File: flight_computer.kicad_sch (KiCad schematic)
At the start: 2 parts

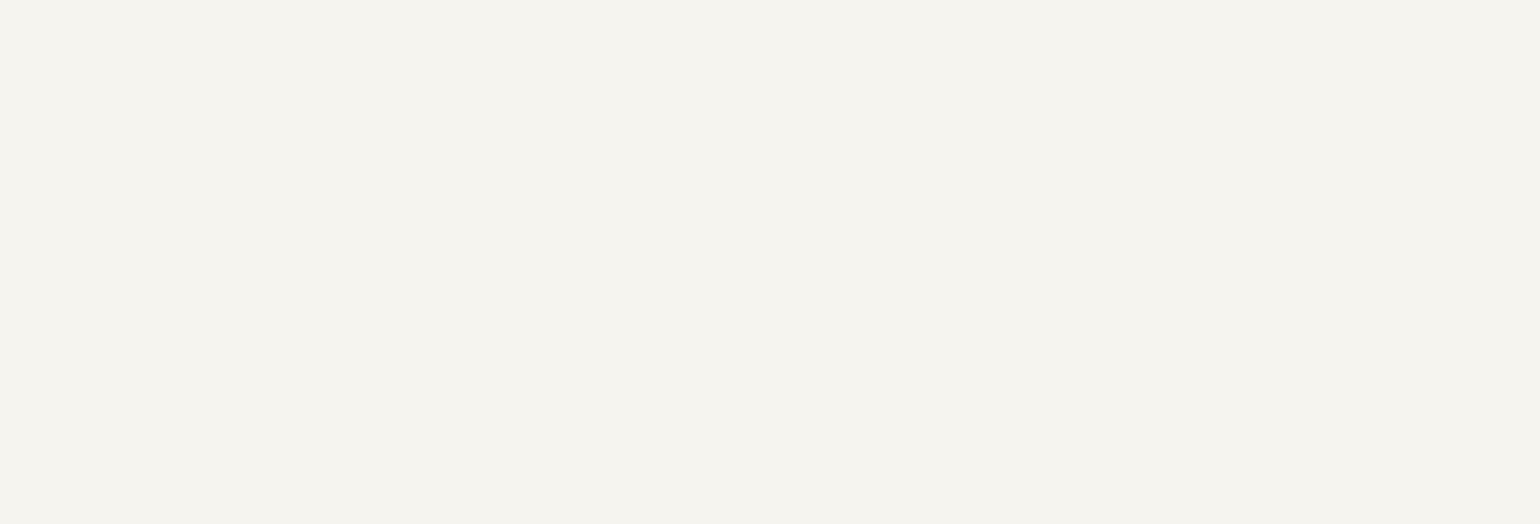
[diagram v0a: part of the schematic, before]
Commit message: Major fix: move from a flat to a hierarchical architecture for schematic.
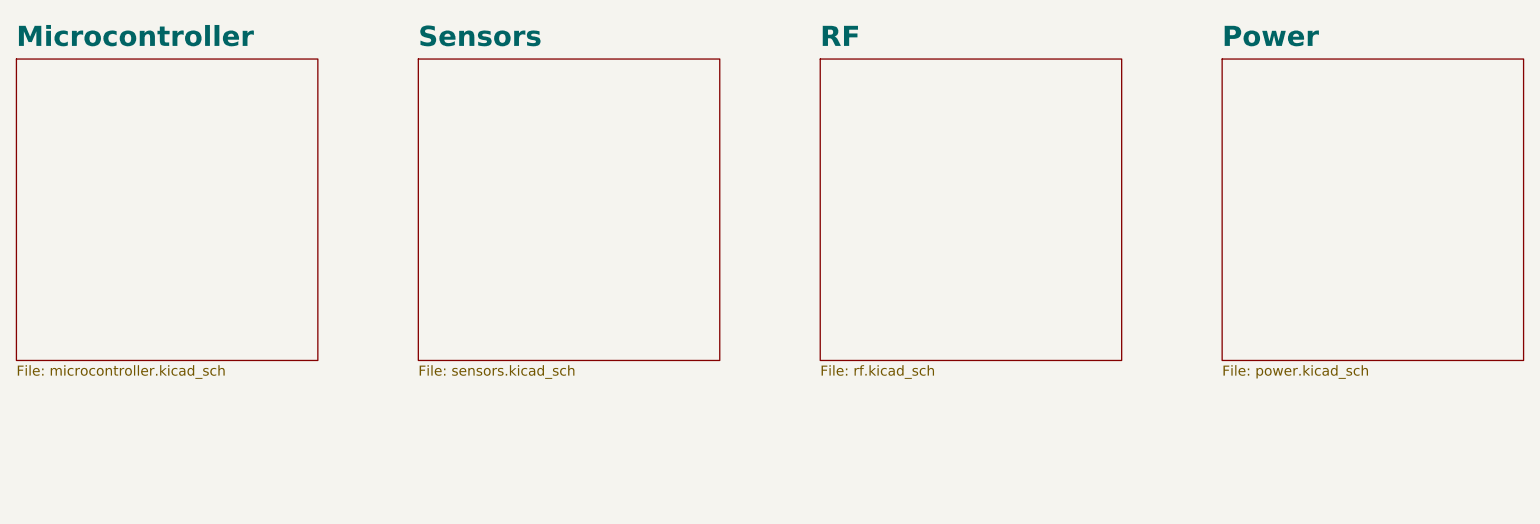
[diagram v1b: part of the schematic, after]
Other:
- added sheet Microcontroller (microcontroller.kicad_sch)
- added sheet Power (power.kicad_sch)
- added sheet RF (rf.kicad_sch)
- added sheet Sensors (sensors.kicad_sch)
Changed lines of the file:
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@@
+		)
+	)
+	(sheet
+		(at 177.8 25.4)
+		(size 38.1 38.1)
+		(exclude_from_sim no)
+		(in_bom yes)
+		(on_board yes)
+		(dnp no)
+		(fields_autoplaced yes)
+		(stroke
+			(width 0.1524)
+			(type solid)
+		)
+		(fill
+			(color 0 0 0 0)
+		)
+		(property "Sheetname" "Power"
+			(at 177.8 24.0534 0)
+			(show_name no)
+			(do_not_autoplace no)
+			(effects
+				(font
+					(size 2.54 2.54)
+					(thickness 0.508)
+					(bold yes)
+				)
+				(justify left bottom)
+			)
+		)
+		(property "Sheetfile" "power.kicad_sch"
+			(at 177.8 64.0846 0)
+			(show_name no)
+			(do_not_autoplace no)
+			(effects
+				(font
+					(size 1.27 1.27)
+				)
+				(justify left top)
+			)
+		)
+		(instances
+			(project "flight_computer"
+				(path "/aee43b18-7cf7-43bb-b265-763f492d287e"
+					(page "2")
+				)
+			)
+		)
+	)
+	(sheet
+		(at 25.4 25.4)
+		(size 38.1 38.1)
+		(exclude_from_sim no)
+		(in_bom yes)
+		(on_board yes)
+		(dnp no)
+		(fields_autoplaced yes)
+		(stroke
+			(width 0.1524)
+			(type solid)
+		)
+		(fill
+			(color 0 0 0 0)
+		)
+		(property "Sheetname" "Microcontroller"
+			(at 25.4 24.0534 0)
+			(show_name no)
+			(do_not_autoplace no)
+			(effects
+				(font
+					(size 2.54 2.54)
+					(thickness 0.508)
+					(bold yes)
+				)
+				(justify left bottom)
+			)
+		)
+		(property "Sheetfile" "microcontroller.kicad_sch"
+			(at 25.4 64.0846 0)
+			(show_name no)
+			(do_not_autoplace no)
+			(effects
+				(font
+					(size 1.27 1.27)
+				)
+				(justify left top)
+			)
+		)
+		(instances
+			(project "flight_computer"
+				(path "/aee43b18-7cf7-43bb-b265-763f492d287e"
+					(page "3")
+				)
+			)
+		)
+	)
+	(sheet
+		(at 76.2 25.4)
+		(size 38.1 38.1)
+		(exclude_from_sim no)
+		(in_bom yes)
+		(on_board yes)
+		(dnp no)
+		(fields_autoplaced yes)
+		(stroke
+			(width 0.1524)
+			(type solid)
+		)
+		(fill
+			(color 0 0 0 0)
+		)
+		(property "Sheetname" "Sensors"
+			(at 76.2 24.0534 0)
+			(show_name no)
+			(do_not_autoplace no)
+			(effects
+				(font
+					(size 2.54 2.54)
+					(thickness 0.508)
+					(bold yes)
+				)
+				(justify left bottom)
+			)
+		)
+		(property "Sheetfile" "sensors.kicad_sch"
+			(at 76.2 64.0846 0)
+			(show_name no)
+			(do_not_autoplace no)
+			(effects
+				(font
+					(size 1.27 1.27)
+				)
+				(justify left top)
+			)
+		)
+		(instances
+			(project "flight_computer"
+				(path "/aee43b18-7cf7-43bb-b265-763f492d287e"
+					(page "4")
+				)
+			)
+		)
+	)
+	(sheet
+		(at 127 25.4)
+		(size 38.1 38.1)
+		(exclude_from_sim no)
+		(in_bom yes)
+		(on_board yes)
+		(dnp no)
+		(fields_autoplaced yes)
+		(stroke
+			(width 0.1524)
+			(type solid)
+		)
+		(fill
+			(color 0 0 0 0)
+		)
+		(property "Sheetname" "RF"
+			(at 127 24.0534 0)
+			(show_name no)
+			(do_not_autoplace no)
+			(effects
+				(font
+					(size 2.54 2.54)
+					(thickness 0.508)
+					(bold yes)
+				)
+				(justify left bottom)
+			)
+		)
+		(property "Sheetfile" "rf.kicad_sch"
+			(at 127 64.0846 0)
+			(show_name no)
+			(do_not_autoplace no)
+			(effects
+				(font
+					(size 1.27 1.27)
+				)
+				(justify left top)
+			)
+		)
+		(instances
+			(project "flight_computer"
+				(path "/aee43b18-7cf7-43bb-b265-763f492d287e"
+					(page "5")
+				)
+			)
 		)
 	)

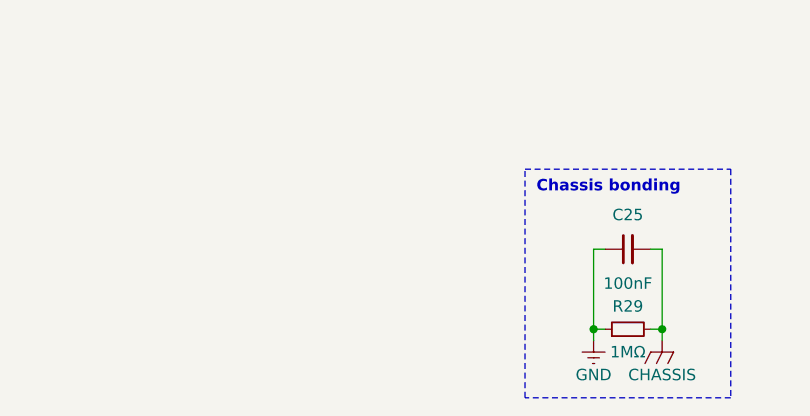
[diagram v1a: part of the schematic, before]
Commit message: Added M3 mounting holes to schematic, replaced them in PCB layout so they appear in the output documents
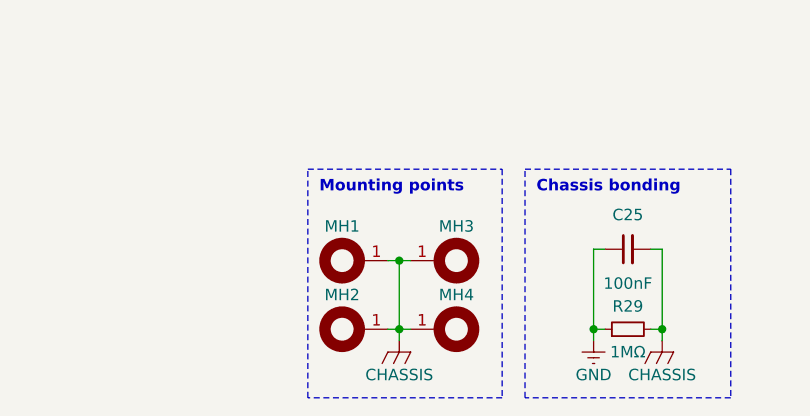
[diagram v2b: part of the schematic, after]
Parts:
- added MH1, MH2, MH3, MH4: (no value), miscellaneous:M3, symbol miscellaneous:M3
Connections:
- net CHASSIS: now also MH1.1 (MH), MH2.1 (MH), MH3.1 (MH), MH4.1 (MH)
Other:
- note added: "Mounting points"
